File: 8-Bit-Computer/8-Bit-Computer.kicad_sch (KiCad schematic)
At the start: 10 parts, among them U1 NA555D, U2 AMS1117-5.0, U3 74HC00

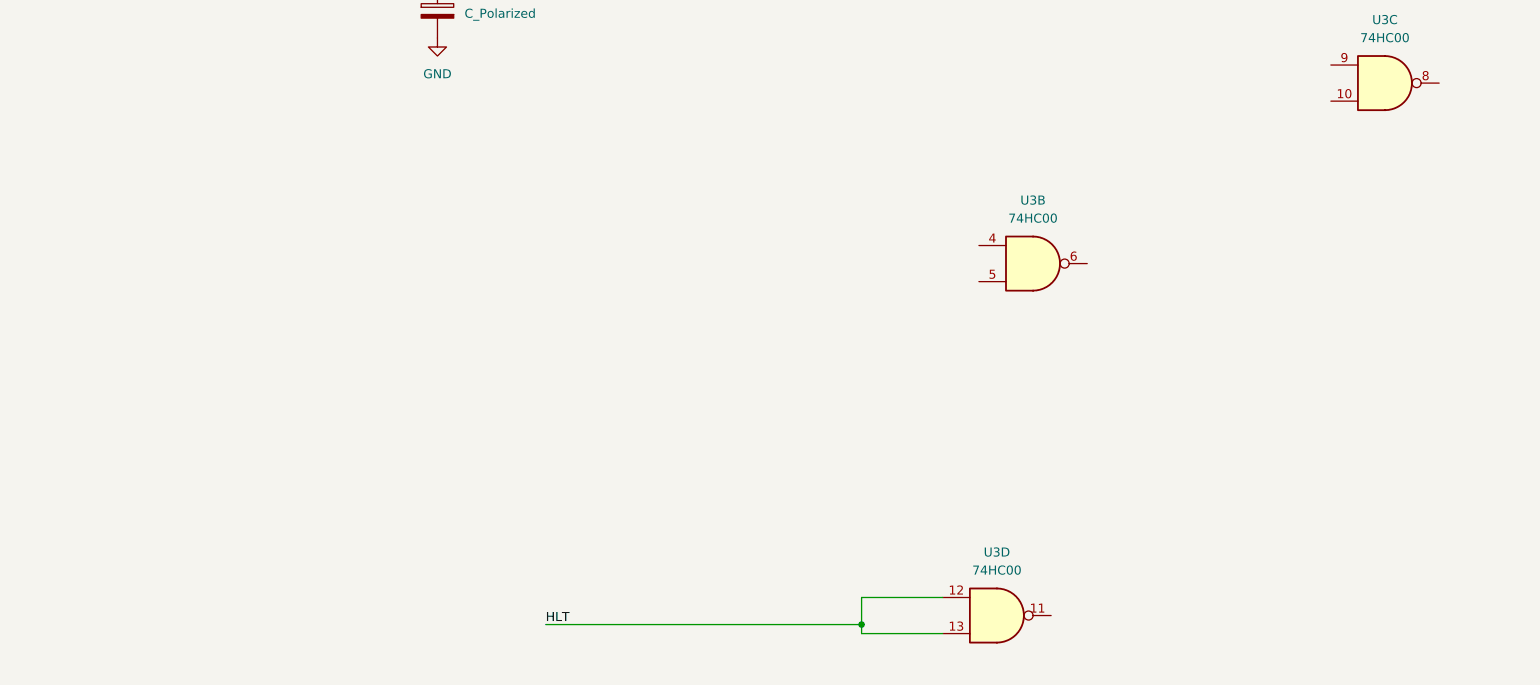
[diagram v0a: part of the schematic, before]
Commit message: finished monostable
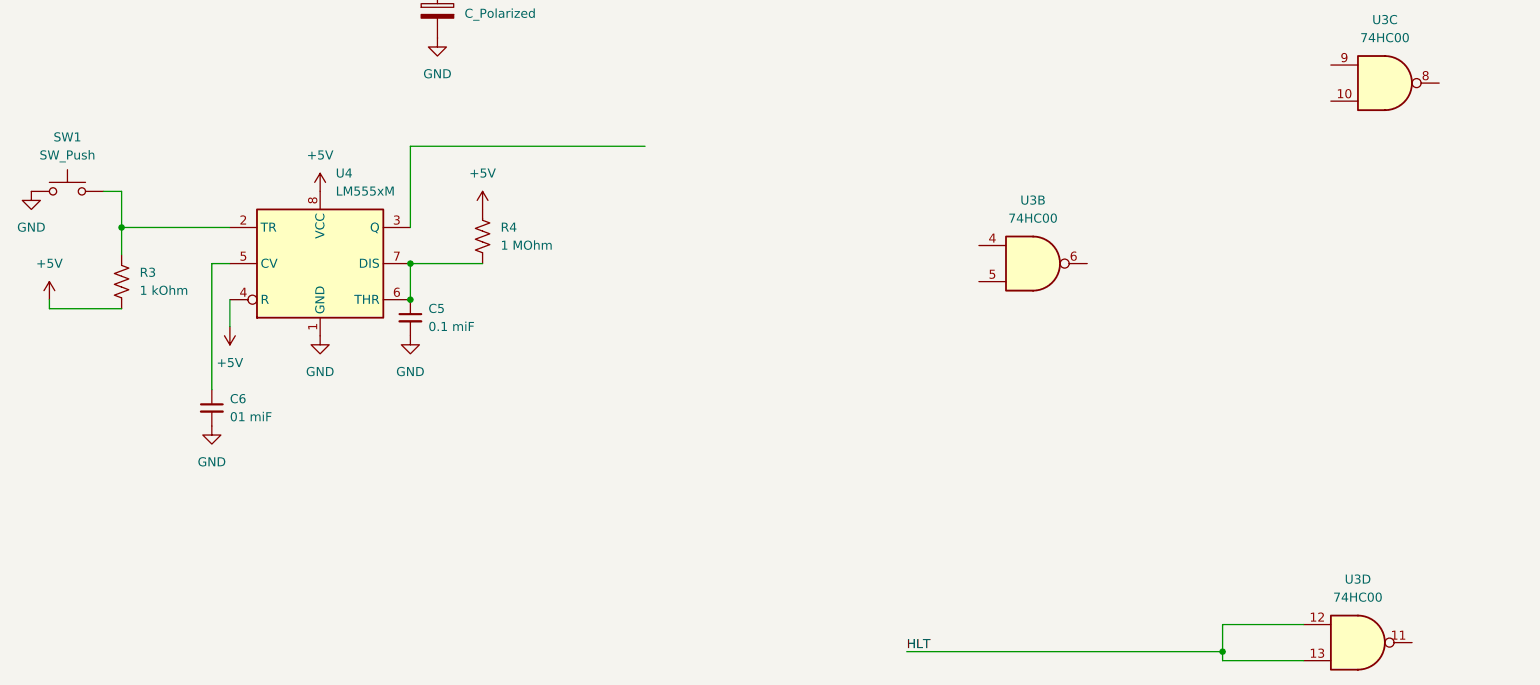
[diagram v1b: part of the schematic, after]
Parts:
- added C5: 0.1 miF, symbol Device:C_Small
- added C6: 01 miF, symbol Device:C_Small
- added R3: 1 kOhm, symbol Device:R_US
- added R4: 1 MOhm, symbol Device:R_US
- added SW1: SW_Push, symbol Switch:SW_Push
- added U4: LM555xM, Package_SO:SOIC-8_3.9x4.9mm_P1.27mm, symbol Timer:LM555xM
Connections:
- net +5V: now also R3.2, R4.1, U4.4 (R), U4.8 (VCC)
- net GND: now also C5.2, C6.2, SW1.1, U4.1 (GND)
- new net: R3.1, SW1.2, U4.2 (TR)
- new net: C6.1, U4.5 (CV)
- new net: C5.1, R4.2, U4.6 (THR), U4.7 (DIS)
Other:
- moved on the sheet: U3D

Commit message: finished clock module
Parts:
- added C7: 0.1 miF, symbol Device:C_Small
- added J1: XLR3_Switched, symbol Connector_Audio:XLR3_Switched
- added R5: R_US, symbol Device:R_US
- added R6: 1 kOhm, symbol Device:R_US
- added U5: NA555D, Package_SO:SOIC-8_3.9x4.9mm_P1.27mm, symbol Timer:NA555D
- added U6: 74HC00, symbol 74xx:74HC00
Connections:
- net +5V: now also U3.14 (VCC), R5.1, R6.2, U5.8 (VCC), U6.14 (VCC)
- net GND: now also U3.7 (GND), C7.2, J1.N, U5.1 (GND), U5.6 (THR), U6.7 (GND)
- net at U3.10: now also U3.2, U3.9, U5.3 (Q)
- net at U3.8: now also U3.4
- net at U4.3 (Q): now also U3.5
- net at U3.6: now also U6.2
- net at U1.3 (Q): now also U3.1
- net at U3.3: now also U6.1
- net at U3.11: now also U6.5
- new net: J1.NC, R5.2, U5.2 (TR)
- new net: J1.NO, R6.1, U5.4 (R)
- new net: U6.3, U6.4
- new net: U6.10, U6.6, U6.9
- new net: C7.1, U5.5 (CV)
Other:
- moved on the sheet: U3B, U3C, U3D

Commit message: working on alu
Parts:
- added REGA, REGB: 74HC273, symbol 74xx:74HC273
- added U7, U8: 74HC245, symbol 74xx:74HC245
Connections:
- net +5V: now also REGA.20 (VCC), REGB.20 (VCC), U7.1 (A->B), U7.20 (VCC), U8.1 (A->B), U8.20 (VCC)
- net GND: now also REGA.10 (GND), REGB.10 (GND), U7.10 (GND), U7.19 (CE), U8.10 (GND), U8.19 (CE)
- net clock_pulse: now reaches U6.8
- net clock_pulse: now also REGA.11 (Cp), REGB.11 (Cp)
- new net: REGB.12 (Q4), U8.6 (A4)
- new net: REGB.15 (Q5), U8.7 (A5)
- new net: REGB.16 (Q6), U8.8 (A6)
- new net: REGB.19 (Q7), U8.9 (A7)
- new net: REGB.2 (Q0), U8.2 (A0)
- new net: REGB.5 (Q1), U8.3 (A1)
- new net: REGB.6 (Q2), U8.4 (A2)
- new net: REGB.9 (Q3), U8.5 (A3)
- new net: REGA.2 (Q0), U7.2 (A0)
- new net: REGA.5 (Q1), U7.3 (A1)
- new net: REGA.6 (Q2), U7.4 (A2)
- new net: REGA.9 (Q3), U7.5 (A3)
- new net: REGA.12 (Q4), U7.6 (A4)
- new net: REGA.15 (Q5), U7.7 (A5)
- new net: REGA.16 (Q6), U7.8 (A6)
- new net: REGA.19 (Q7), U7.9 (A7)
- new net Reset: REGA.1 (~{Mr}), REGB.1 (~{Mr})
- no-connect marks 0 -> 1

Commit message: ALU done
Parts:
- added U10, U9: 74LS283, symbol 74xx:74LS283
- added U11: 74HC245, symbol 74xx:74HC245
- added U12, U13: 74HC86, symbol 74xx:74HC86
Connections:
- net +5V: now also U10.16 (VCC), U11.1 (A->B), U11.20 (VCC), U12.14 (VCC), U13.14 (VCC), U9.16 (VCC)
- net GND: now also U10.8 (GND), U11.10 (GND), U12.7 (GND), U13.7 (GND), U9.8 (GND); no longer U7.19 (CE), U8.19 (CE)
- net at REGB.12 (Q4), U8.6 (A4): now also U13.2
- net at REGB.15 (Q5), U8.7 (A5): now also U13.5
- net at REGB.16 (Q6), U8.8 (A6): now also U13.10
- net at REGB.19 (Q7), U8.9 (A7): now also U13.13
- net at REGB.2 (Q0), U8.2 (A0): now also U12.13
- net at REGB.5 (Q1), U8.3 (A1): now also U12.10
- net at REGB.6 (Q2), U8.4 (A2): now also U12.5
- net at REGB.9 (Q3), U8.5 (A3): now also U12.2
- net at REGA.2 (Q0), U7.2 (A0): now also U9.5 (A1)
- net at REGA.5 (Q1), U7.3 (A1): now also U9.3 (A2)
- net at REGA.6 (Q2), U7.4 (A2): now also U9.14 (A3)
- net at REGA.9 (Q3), U7.5 (A3): now also U9.12 (A4)
- net at REGA.12 (Q4), U7.6 (A4): now also U10.5 (A1)
- net at REGA.15 (Q5), U7.7 (A5): now also U10.3 (A2)
- net at REGA.16 (Q6), U7.8 (A6): now also U10.14 (A3)
- net at REGA.19 (Q7), U7.9 (A7): now also U10.12 (A4)
- new net: U12.3, U9.11 (B4)
- new net: U10.6 (B1), U13.3
- new net: U12.11, U9.6 (B1)
- new net: U11.2 (A0), U9.4 (S1)
- new net: U11.3 (A1), U9.1 (S2)
- new net: U11.4 (A2), U9.13 (S3)
- new net: U11.5 (A3), U9.10 (S4)
- new net: U10.4 (S1), U11.6 (A4)
- new net: U10.1 (S2), U11.7 (A5)
- new net: U10.13 (S3), U11.8 (A6)
- new net: U10.10 (S4), U11.9 (A7)
- new net: U10.11 (B4), U13.11
- new net: U12.6, U9.15 (B3)
- new net: U12.8, U9.2 (B2)
- new net: U10.7 (C0), U9.9 (C4)
- new net: U10.15 (B3), U13.8
- new net: U10.2 (B2), U13.6
- new net Aout: U7.19 (CE)
- new net Bout: U8.19 (CE)
- new net SUB: U12.1, U12.12, U12.4, U12.9, U13.1, U13.12, U13.4, U13.9, U9.7 (C0)
- new net Sout: U11.19 (CE)
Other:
- moved on the sheet: REGA, REGB, U7, U8

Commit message: not done much
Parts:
- added U15: HM62256BLP, Package_DIP:DIP-28_W15.24mm, symbol Memory_RAM:HM62256BLP
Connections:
- net +5V: now also U15.28 (VCC)
- net GND: now also U15.14 (GND)
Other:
- note added: "ALU and Registers"
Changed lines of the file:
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@@
     (effects (font (size 1.27 1.27)) (justify left top))
+  )
+  (text "ALU and Registers" (at 42.545 252.095 0)
+    (effects (font (size 1.27 1.27)) (justify left bottom))
   )
   (label "clock_pulse" (at 45.72 450.85 180) (fields_autoplaced)
@@
     )
   )
+  (symbol (lib_id "power:+5V") (at 542.29 274.32 180) (unit 1)
+    (in_bom yes) (on_board yes) (dnp no) (fields_autoplaced)
+    (property "Reference" "#PWR033" (at 542.29 270.51 0)
+      (effects (font (size 1.27 1.27)) hide)
+    )
+    (property "Value" "+5V" (at 542.29 279.4 0)
+      (effects (font (size 1.27 1.27)))
+    )
+    (property "Footprint" "" (at 542.29 274.32 0)
+      (effects (font (size 1.27 1.27)) hide)
+    )
+    (property "Datasheet" "" (at 542.29 274.32 0)
+      (effects (font (size 1.27 1.27)) hide)
+    )
+    (pin "1")
+    (instances
+      (project "8-Bit-Computer"
+        (path "/7068cf22-ceca-4c5f-b7d5-56f579bc3b1d"
+          (reference "#PWR033") (unit 1)
+        )
+      )
+    )
+  )
   (symbol (lib_id "74xx:74HC86") (at 53.975 389.89 0) (unit 3)
     (in_bom yes) (on_board yes) (dnp no) (fields_autoplaced)
@@
         (path "/7068cf22-ceca-4c5f-b7d5-56f579bc3b1d"
           (reference "U1") (unit 1)
+        )
+      )
+    )
+  )
+  (symbol (lib_id "power:GND") (at 542.29 228.6 180) (unit 1)
+    (in_bom yes) (on_board yes) (dnp no) (fields_autoplaced)
+    (property "Reference" "#PWR039" (at 542.29 222.25 0)
+      (effects (font (size 1.27 1.27)) hide)
+    )
+    (property "Value" "GND" (at 542.29 223.52 0)
+      (effects (font (size 1.27 1.27)))
+    )
+    (property "Footprint" "" (at 542.29 228.6 0)
+      (effects (font (size 1.27 1.27)) hide)
+    )
+    (property "Datasheet" "" (at 542.29 228.6 0)
+      (effects (font (size 1.27 1.27)) hide)
+    )
+    (pin "1")
+    (instances
+      (project "8-Bit-Computer"
+        (path "/7068cf22-ceca-4c5f-b7d5-56f579bc3b1d"
+          (reference "#PWR039") (unit 1)
         )
       )
@@
         )
       )
+    )
+  )
+  (symbol (lib_id "Memory_RAM:HM62256BLP") (at 542.29 251.46 180) (unit 1)
+    (in_bom yes) (on_board yes) (dnp no) (fields_autoplaced)
+    (property "Reference" "U15" (at 540.0959 276.86 0)
+      (effects (font (size 1.27 1.27)) (justify left))
+    )
+    (property "Value" "HM62256BLP" (at 540.0959 274.32 0)
+      (effects (font (size 1.27 1.27)) (justify left))
+    )
+    (property "Footprint" "Package_DIP:DIP-28_W15.24mm" (at 542.29 248.92 0)
+      (effects (font (size 1.27 1.27)) hide)
+    )
+    (property "Datasheet" "https://web.mit.edu/6.115/www/document/62256.pdf" (at 542.29 248.92 0)
+      (effects (font (size 1.27 1.27)) hide)
+    )
+    (pin "2")
+    (pin "16")
+    (pin "24")
+    (pin "5")
+    (pin "18")
+    (pin "4")
+    (pin "26")
+    (pin "23")
+    (pin "21")
+    (pin "3")
+    (pin "9")
+    (pin "20")
+    (pin "22")
+    (pin "11")
+    (pin "15")
+    (pin "8")
+    (pin "28")
+    (pin "12")
+    (pin "1")
+    (pin "14")
+    (pin "17")
+    (pin "25")
+    (pin "27")
+    (pin "19")
+    (pin "13")
+    (pin "6")
+    (pin "7")
+    (pin "10")
+    (instances
+      (project "8-Bit-Computer"
+        (path "/7068cf22-ceca-4c5f-b7d5-56f579bc3b1d"
+          (reference "U15") (unit 1)
+        )
+      )

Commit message: still working on mem
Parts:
- added J2: XLR3_Switched, symbol Connector_Audio:XLR3_Switched
- added R10, R11, R8, R9: R_US, symbol Device:R_US
- added SW2: SW_DIP_x04, symbol Switch:SW_DIP_x04
- added U14, U16: 74HC245, symbol 74xx:74HC245
- added U17, U18, U19, U21: 74157, symbol 74xx_IEEE:74157
- added U20: 74HC00, symbol 74xx:74HC00
- added U22: 74173, symbol 74xx_IEEE:74173
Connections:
- net +5V: now also R10.2, R11.2, R8.2, R9.2, U14.20 (VCC), U16.1 (A->B), U16.20 (VCC), U21.16 (VCC), U22.16 (VCC)
- net GND: now also U15.1 (A14), U15.2 (A12), U15.20 (~{CS}), U15.21 (A10), U15.22 (~{OE}), U15.23 (A11), U15.24 (A9), U15.25 (A8), U15.26 (A13), U15.3 (A7), U15.4 (A6), U15.5 (A5), U15.6 (A4), J2.N, SW2.5, SW2.6, SW2.7, SW2.8, U14.1 (A->B), U14.10 (GND), U16.10 (GND), U21.15 (~{EN}), U21.8 (GND), U22.1 (~{M}), U22.15 (R), U22.2 (~{N}), U22.8 (GND)
- net clock_pulse: now also U22.7 (CK)
- net at U15.10 (A0): now also U21.4 (Qa)
- net at U15.11 (Q0): now also U14.2 (A0), U16.2 (A0)
- net at U15.12 (Q1): now also U14.3 (A1), U16.3 (A1)
- net at U15.13 (Q2): now also U14.4 (A2), U16.4 (A2)
- net at U15.15 (Q3): now also U14.5 (A3), U16.5 (A3)
- net at U15.16 (Q4): now also U14.6 (A4), U16.6 (A4)
- net at U15.17 (Q5): now also U14.7 (A5), U16.7 (A5)
- net at U15.18 (Q6): now also U14.8 (A6), U16.8 (A6)
- net at U15.19 (Q7): now also U14.9 (A7), U16.9 (A7)
- net at U15.27 (~{WE}): now also U14.19 (CE)
- net at U15.7 (A3): now also U21.9 (Qd)
- net at U15.8 (A2): now also U21.12 (Qc)
- net at U15.9 (A1): now also U21.7 (Qb)
- net Aout renamed #Aout
- net Bout renamed #Bout
- net Sout renamed #Sout
- new net: U21.2 (I0a), U22.3 (Q0)
- new net: U21.5 (I0b), U22.4 (Q1)
- new net: U21.14 (I0c), U22.5 (Q2)
- new net: U21.11 (I0d), U22.6 (Q3)
- new net: R9.1, SW2.1, U21.10 (I1d)
- new net: R8.1, SW2.2, U21.13 (I1c)
- new net: R10.1, SW2.3, U21.6 (I1b)
- new net: R11.1, SW2.4, U21.3 (I1a)
- new net #MEM_O: U16.19 (CE)
- new net A_in: U22.10 (~{G2}), U22.9 (~{G1})

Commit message: working on mem
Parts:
- added D1: G_LED, symbol Device:LED
- added D2: R_LED, symbol Device:LED
- added R12, R7: R_US, symbol Device:R_US
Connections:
- net +5V: now also R12.2, R7.2
- net at U21.1 (A/B): now also J2.NC, D1.2 (A)
- net at J2.NO: now also D2.2 (A)
- net A_in renamed Addr_in
- new net: D2.1 (K), R12.1
- new net: D1.1 (K), R7.1
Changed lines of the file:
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@@
   (junction (at 520.7 256.54) (diameter 0) (color 0 0 0 0)
   )
+  (junction (at 515.62 103.505) (diameter 0) (color 0 0 0 0)
+  )
   (junction (at 481.33 166.37) (diameter 0) (color 0 0 0 0)
   )
@@
     (stroke (width 0) (type default))
   )
+  (wire (pts (xy 515.62 99.695) (xy 515.62 103.505))
+    (stroke (width 0) (type default))
+  )
   (wire (pts (xy 411.48 191.135) (xy 421.64 191.135))
     (stroke (width 0) (type default))
@@
     (stroke (width 0) (type default))
   )
+  (wire (pts (xy 510.54 99.695) (xy 510.54 104.775))
+    (stroke (width 0) (type default))
+  )
   (wire (pts (xy 219.71 158.75) (xy 330.2 158.75))
     (stroke (width 0) (type default))
@@
     (stroke (width 0) (type default))
   )
+  (wire (pts (xy 515.62 103.505) (xy 515.62 142.875))
+    (stroke (width 0) (type default))
+  )
   (wire (pts (xy 61.595 389.89) (xy 73.66 389.89))
     (stroke (width 0) (type default))
@@
     (stroke (width 0) (type default))
   )
+  (wire (pts (xy 506.095 104.775) (xy 510.54 104.775))
+    (stroke (width 0) (type default))
+  )
   (wire (pts (xy 529.59 254) (xy 520.065 254))
     (stroke (width 0) (type default))
@@
     (stroke (width 0) (type default))
   )
+  (wire (pts (xy 515.62 142.875) (xy 521.97 142.875))
+    (stroke (width 0) (type default))
+  )
   (wire (pts (xy 554.99 243.84) (xy 554.99 246.38))
     (stroke (width 0) (type default))
@@
     (effects (font (size 1.27 1.27)) (justify right bottom))
   )
-  (label "A_in" (at 411.48 186.055 180) (fields_autoplaced)
+  (label "Addr_in" (at 411.48 186.055 180) (fields_autoplaced)
     (effects (font (size 1.27 1.27)) (justify right bottom))
   )
@@
     )
   )
+  (symbol (lib_id "Device:R_US") (at 506.095 116.205 0) (unit 1)
+    (in_bom yes) (on_board yes) (dnp no) (fields_autoplaced)
+    (property "Reference" "R12" (at 511.81 116.205 90)
+      (effects (font (size 1.27 1.27)))
+    )
+    (property "Value" "R_US" (at 509.27 116.205 90)
+      (effects (font (size 1.27 1.27)))
+    )
+    (property "Footprint" "" (at 507.111 116.459 90)
+      (effects (font (size 1.27 1.27)) hide)
+    )
+    (property "Datasheet" "~" (at 506.095 116.205 0)
+      (effects (font (size 1.27 1.27)) hide)
+    )
+    (pin "2")
+    (pin "1")
+    (instances
+      (project "8-Bit-Computer"
+        (path "/7068cf22-ceca-4c5f-b7d5-56f579bc3b1d"
+          (reference "R12") (unit 1)
+        )
+      )
+    )
+  )
   (symbol (lib_id "Connector_Audio:XLR3_Switched") (at 49.53 232.41 90) (unit 2)
     (in_bom yes) (on_board yes) (dnp no) (fields_autoplaced)
@@
     )
   )
+  (symbol (lib_id "Device:LED") (at 506.095 108.585 90) (unit 1)
+    (in_bom yes) (on_board yes) (dnp no)
+    (property "Reference" "D2" (at 513.08 110.1725 0)
+      (effects (font (size 1.27 1.27)))
+    )
+    (property "Value" "R_LED" (at 510.54 110.1725 0)
+      (effects (font (size 1.27 1.27)))
+    )
+    (property "Footprint" "" (at 506.095 108.585 0)
+      (effects (font (size 1.27 1.27)) hide)
+    )
+    (property "Datasheet" "~" (at 506.095 108.585 0)
+      (effects (font (size 1.27 1.27)) hide)
+    )
+    (pin "2")
+    (pin "1")
+    (instances
+      (project "8-Bit-Computer"
+        (path "/7068cf22-ceca-4c5f-b7d5-56f579bc3b1d"
+          (reference "D2") (unit 1)
+        )
+      )
+    )
+  )
   (symbol (lib_id "74xx:74HC00") (at 212.09 100.33 0) (unit 2)
     (in_bom yes) (on_board yes) (dnp no) (fields_autoplaced)
@@
     )
   )
+  (symbol (lib_id "power:+5V") (at 530.86 103.505 270) (unit 1)
+    (in_bom yes) (on_board yes) (dnp no) (fields_autoplaced)
+    (property "Reference" "#PWR074" (at 527.05 103.505 0)
+      (effects (font (size 1.27 1.27)) hide)
+    )
+    (property "Value" "+5V" (at 534.67 103.505 90)
+      (effects (font (size 1.27 1.27)) (justify left))
+    )
+    (property "Footprint" "" (at 530.86 103.505 0)
+      (effects (font (size 1.27 1.27)) hide)
+    )
+    (property "Datasheet" "" (at 530.86 103.505 0)
+      (effects (font (size 1.27 1.27)) hide)
+    )
+    (pin "1")
+    (instances
+      (project "8-Bit-Computer"
+        (path "/7068cf22-ceca-4c5f-b7d5-56f579bc3b1d"
+          (reference "#PWR074") (unit 1)
+        )
+      )
+    )
+  )
   (symbol (lib_id "power:GND") (at 154.305 438.785 0) (unit 1)
     (in_bom yes) (on_board yes) (dnp no) (fields_autoplaced)
@@
     )
   )
+  (symbol (lib_id "Device:R_US") (at 527.05 103.505 90) (unit 1)
+    (in_bom yes) (on_board yes) (dnp no) (fields_autoplaced)
+    (property "Reference" "R7" (at 527.05 97.79 90)
+      (effects (font (size 1.27 1.27)))
+    )
+    (property "Value" "R_US" (at 527.05 100.33 90)
+      (effects (font (size 1.27 1.27)))
+    )
+    (property "Footprint" "" (at 527.304 102.489 90)
+      (effects (font (size 1.27 1.27)) hide)
+    )
+    (property "Datasheet" "~" (at 527.05 103.505 0)
+      (effects (font (size 1.27 1.27)) hide)
+    )
+    (pin "2")
+    (pin "1")
+    (instances
+      (project "8-Bit-Computer"
+        (path "/7068cf22-ceca-4c5f-b7d5-56f579bc3b1d"
+          (reference "R7") (unit 1)
+        )
+      )
+    )
+  )
   (symbol (lib_id "power:GND") (at 490.22 236.22 180) (unit 1)
     (in_bom yes) (on_board yes) (dnp no) (fields_autoplaced)
@@
     )
   )
+  (symbol (lib_id "Device:LED") (at 519.43 103.505 180) (unit 1)
+    (in_bom yes) (on_board yes) (dnp no)
+    (property "Reference" "D1" (at 521.0175 96.52 0)
+      (effects (font (size 1.27 1.27)))
+    )
+    (property "Value" "G_LED" (at 521.0175 99.06 0)
+      (effects (font (size 1.27 1.27)))
+    )
+    (property "Footprint" "" (at 519.43 103.505 0)
+      (effects (font (size 1.27 1.27)) hide)
+    )
+    (property "Datasheet" "~" (at 519.43 103.505 0)
+      (effects (font (size 1.27 1.27)) hide)
+    )
+    (pin "2")
+    (pin "1")
+    (instances
+      (project "8-Bit-Computer"
+        (path "/7068cf22-ceca-4c5f-b7d5-56f579bc3b1d"
+          (reference "D1") (unit 1)
+        )
+      )
+    )
+  )
   (symbol (lib_id "74xx:74HC00") (at 378.46 86.36 0) (unit 3)
     (in_bom yes) (on_board yes) (dnp no) (fields_autoplaced)
@@
         )
       )
+    )
+  )
+  (symbol (lib_id "power:+5V") (at 506.095 120.015 180) (unit 1)
+    (in_bom yes) (on_board yes) (dnp no) (fields_autoplaced)
+    (property "Reference" "#PWR075" (at 506.095 116.205 0)
+      (effects (font (size 1.27 1.27)) hide)
+    )
+    (property "Value" "+5V" (at 506.095 123.825 90)
+      (effects (font (size 1.27 1.27)) (justify left))
+    )
+    (property "Footprint" "" (at 506.095 120.015 0)
+      (effects (font (size 1.27 1.27)) hide)
+    )
+    (property "Datasheet" "" (at 506.095 120.015 0)
+      (effects (font (size 1.27 1.27)) hide)
+    )
+    (pin "1")
+    (instances
+      (project "8-Bit-Computer"
+        (path "/7068cf22-ceca-4c5f-b7d5-56f579bc3b1d"
+          (reference "#PWR075") (unit 1)
+        )
+      )
